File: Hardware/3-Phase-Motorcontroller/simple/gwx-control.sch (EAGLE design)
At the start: 25 parts, among them IC1 74LS02D, IC2 74LS123D

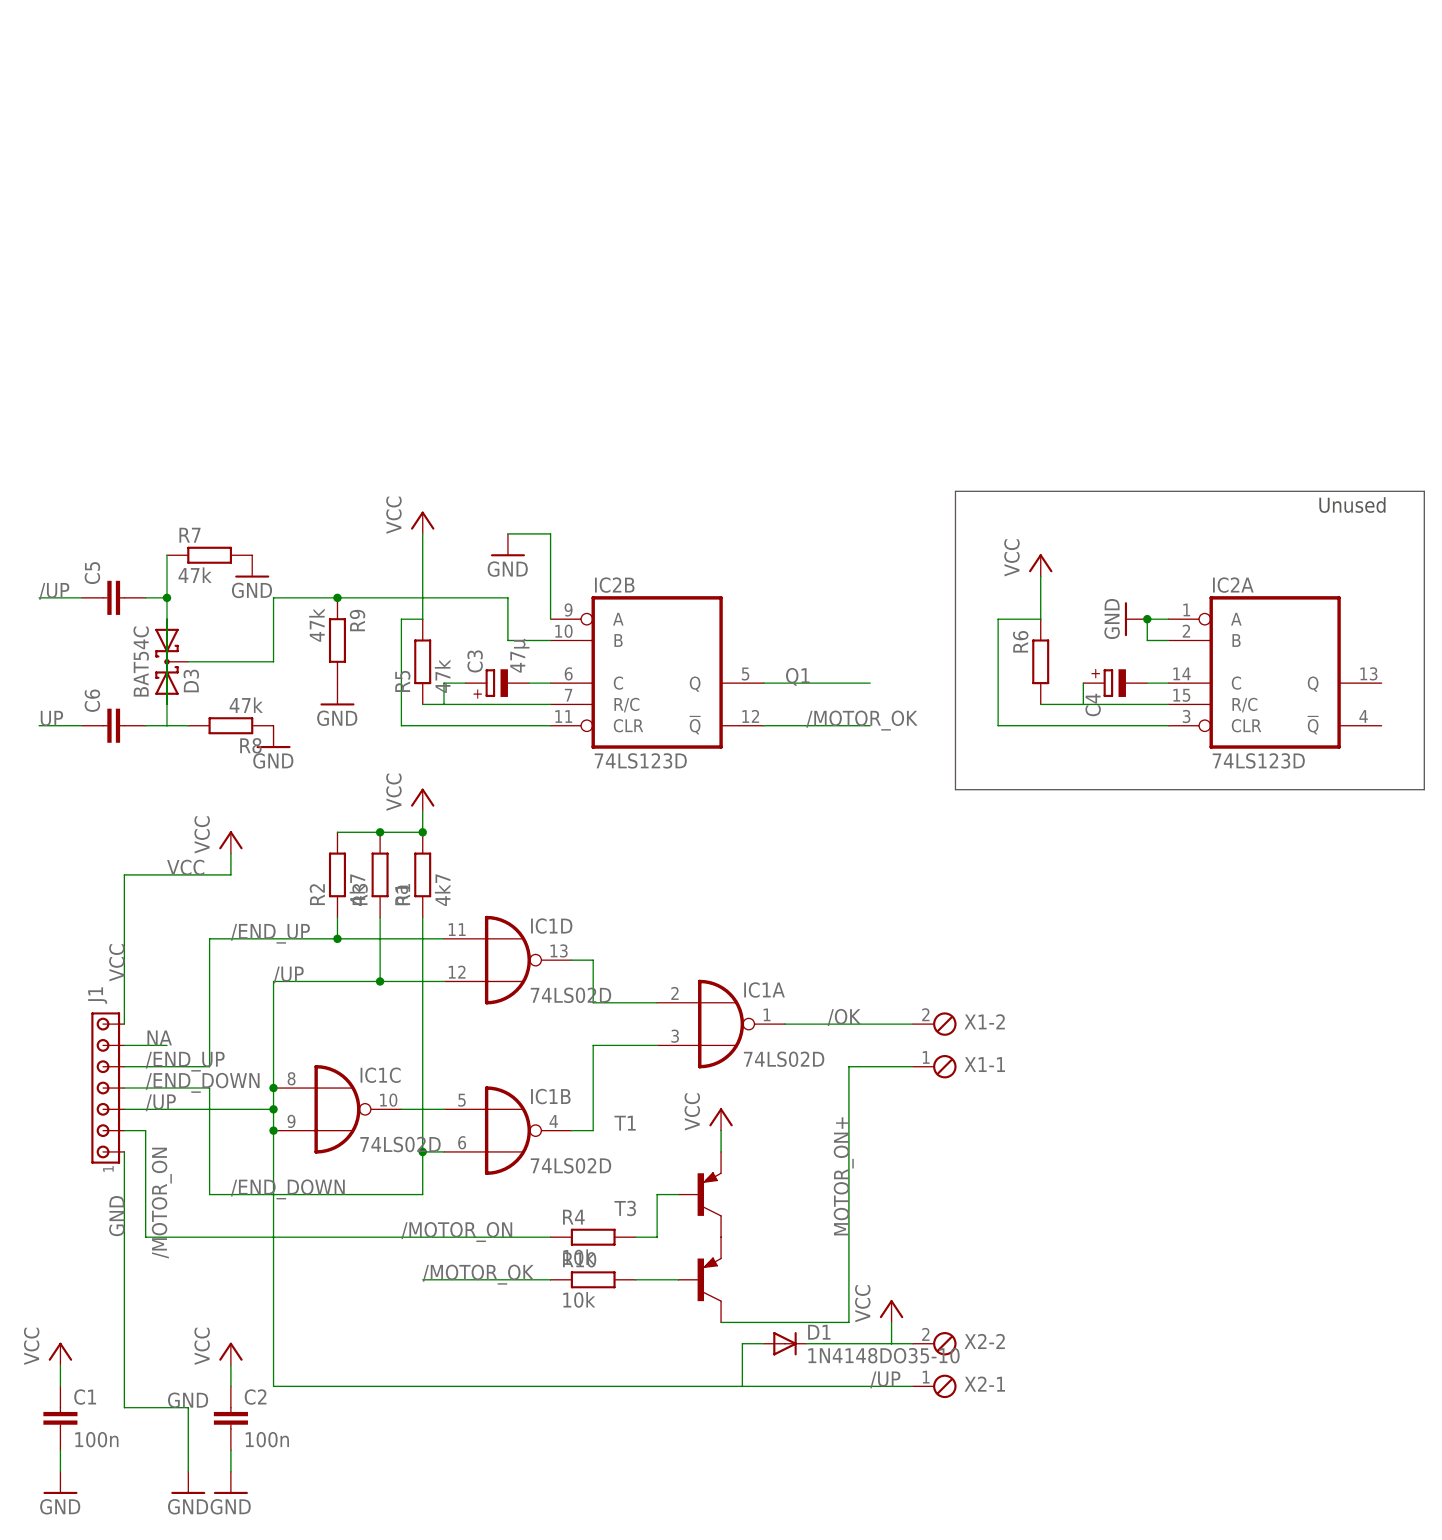
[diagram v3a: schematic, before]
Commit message: Changed Motor force off to non inverted mono flop output
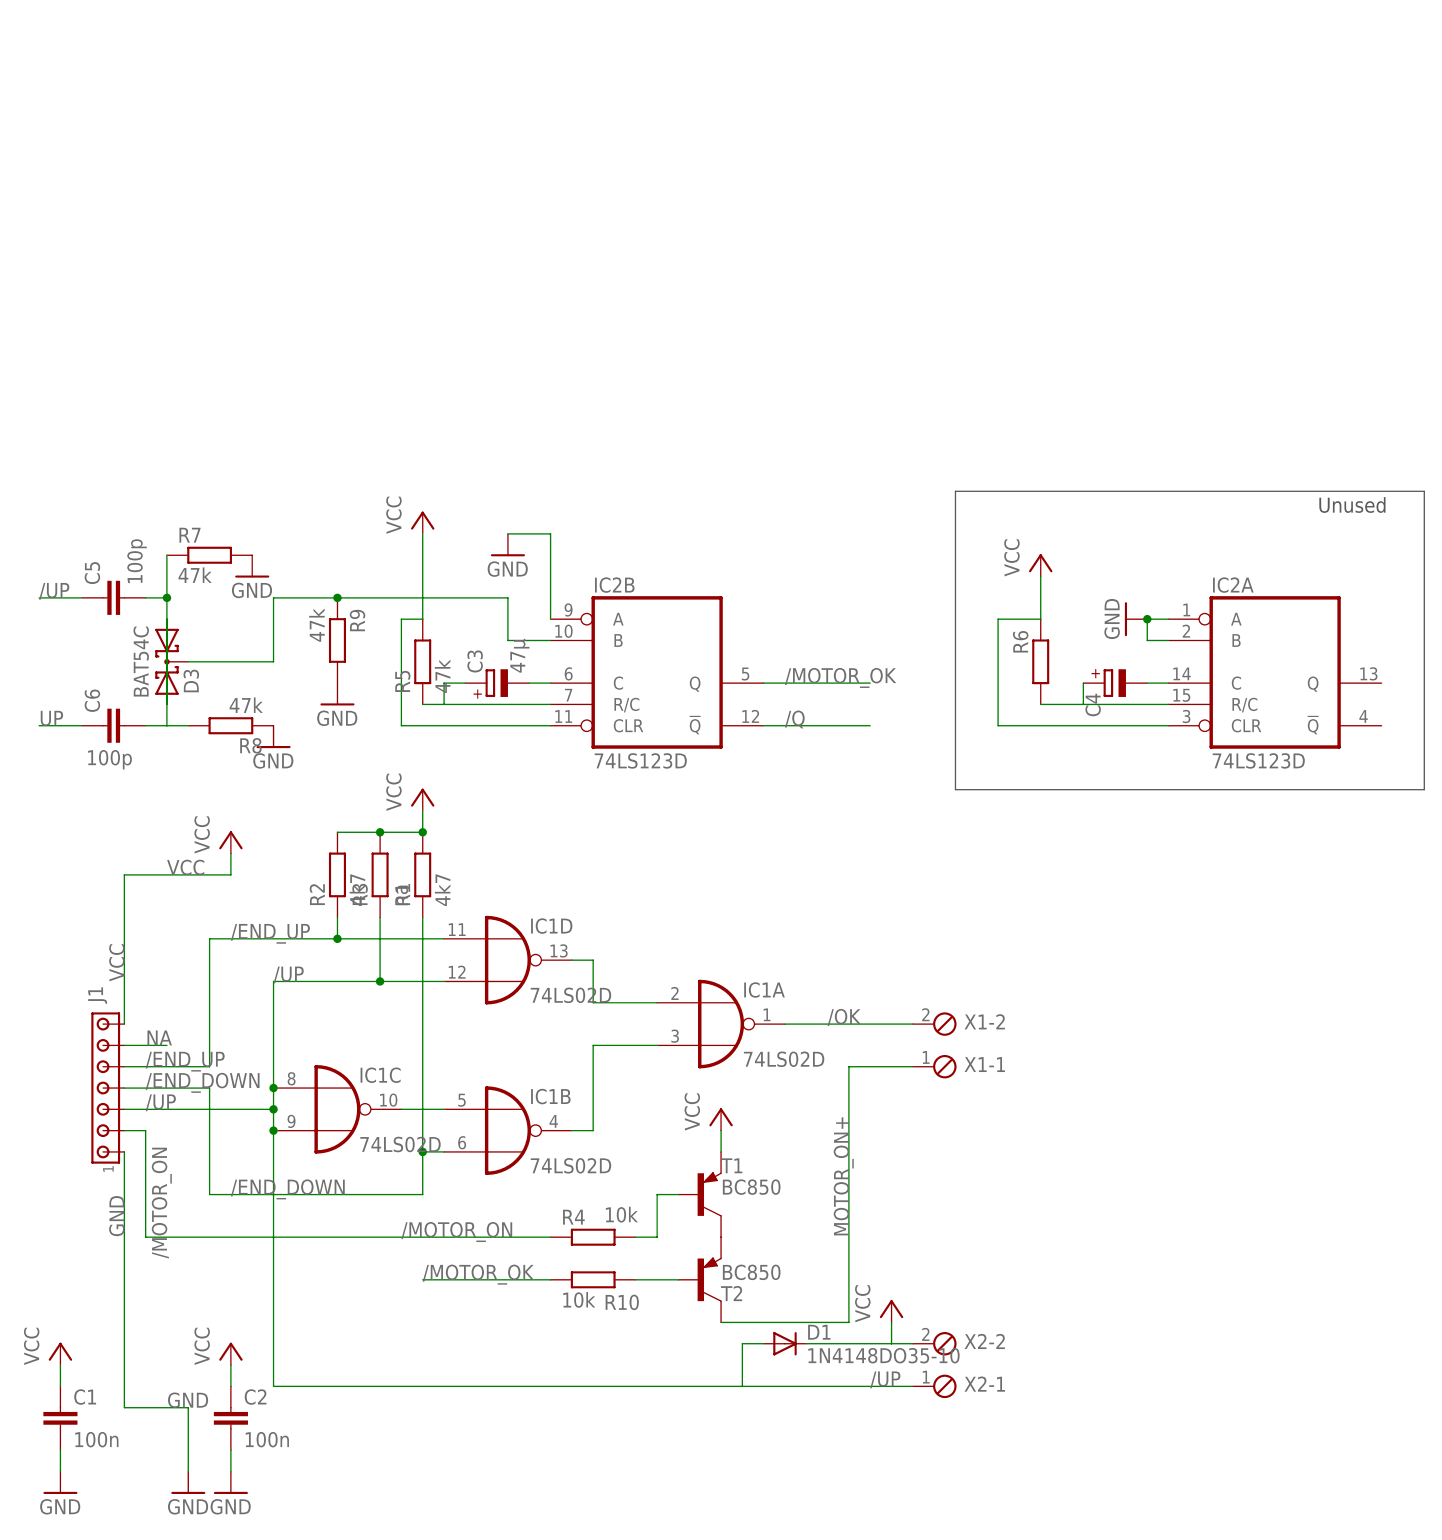
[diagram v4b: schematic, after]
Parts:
- C5, C6: value (none) -> 100p
- T1, T2: value (none) -> BC850
- renumbered T3 to T2
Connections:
- removed net Q1: IC2B.Q
- new net /Q: IC2B.!Q
- net /MOTOR_OK: now also IC2B.Q; no longer IC2B.!Q
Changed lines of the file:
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@@
 <part name="P+4" library="supply1" deviceset="VCC" device=""/>
 <part name="R4" library="resistor" deviceset="R-EU_" device="R0603" value="10k"/>
-<part name="T1" library="transistor" deviceset="*-PNP-" device="SOT23-BEC" technology="BC856B"/>
+<part name="T1" library="transistor" deviceset="*-PNP-" device="SOT23-BEC" technology="BC856B" value="BC850"/>
 <part name="P+5" library="supply1" deviceset="VCC" device=""/>
 <part name="C2" library="rcl" deviceset="C-EU" device="C0603K" value="100n"/>
@@
 <part name="R5" library="rcl" deviceset="R-EU_" device="R0603" value="47k"/>
 <part name="R6" library="rcl" deviceset="R-EU_" device="R0603"/>
-<part name="C5" library="rcl" deviceset="C-EU" device="C0603K"/>
-<part name="C6" library="rcl" deviceset="C-EU" device="C0603K"/>
+<part name="C5" library="rcl" deviceset="C-EU" device="C0603K" value="100p"/>
+<part name="C6" library="rcl" deviceset="C-EU" device="C0603K" value="100p"/>
 <part name="P+7" library="supply1" deviceset="VCC" device=""/>
 <part name="R8" library="rcl" deviceset="R-EU_" device="R0603" value="47k"/>
@@
 <part name="R9" library="rcl" deviceset="R-EU_" device="R0603" value="47k"/>
 <part name="GND8" library="supply1" deviceset="GND" device=""/>
-<part name="T3" library="transistor" deviceset="*-PNP-" device="SOT23-BEC" technology="BC856B"/>
+<part name="T2" library="transistor" deviceset="*-PNP-" device="SOT23-BEC" technology="BC856B" value="BC850"/>
 <part name="R10" library="resistor" deviceset="R-EU_" device="R0603" value="10k"/>
 </parts>
@@
 <instance part="R3" gate="G$1" x="20.32" y="83.82" rot="R90"/>
 <instance part="P+4" gate="VCC" x="25.4" y="93.98"/>
-<instance part="R4" gate="G$1" x="45.72" y="40.64"/>
-<instance part="T1" gate="G$1" x="58.42" y="45.72"/>
+<instance part="R4" gate="G$1" x="45.72" y="40.64" smashed="yes">
+<attribute name="NAME" x="41.91" y="42.1386" size="1.778" layer="95"/>
+<attribute name="VALUE" x="46.99" y="42.418" size="1.778" layer="96"/>
+</instance>
+<instance part="T1" gate="G$1" x="58.42" y="45.72" smashed="yes">
+<attribute name="NAME" x="60.96" y="48.26" size="1.778" layer="95"/>
+<attribute name="VALUE" x="60.96" y="45.72" size="1.778" layer="96"/>
+</instance>
 <instance part="P+5" gate="VCC" x="60.96" y="55.88"/>
 <instance part="C2" gate="G$1" x="2.54" y="20.32"/>
@@
 <instance part="R6" gate="G$1" x="99.06" y="109.22" rot="MR270"/>
 <instance part="C5" gate="G$1" x="-12.7" y="116.84" rot="R90"/>
-<instance part="C6" gate="G$1" x="-12.7" y="101.6" rot="R90"/>
+<instance part="C6" gate="G$1" x="-12.7" y="101.6" smashed="yes" rot="R90">
+<attribute name="NAME" x="-13.081" y="103.124" size="1.778" layer="95" rot="R90"/>
+<attribute name="VALUE" x="-9.144" y="98.679" size="1.778" layer="96" rot="R180"/>
+</instance>
 <instance part="P+7" gate="VCC" x="25.4" y="127"/>
 <instance part="R8" gate="G$1" x="2.54" y="101.6" rot="R180"/>
@@
 <instance part="R9" gate="G$1" x="15.24" y="111.76" rot="R270"/>
 <instance part="GND8" gate="1" x="15.24" y="104.14"/>
-<instance part="T3" gate="G$1" x="58.42" y="35.56"/>
-<instance part="R10" gate="G$1" x="45.72" y="35.56"/>
+<instance part="T2" gate="G$1" x="58.42" y="35.56" smashed="yes">
+<attribute name="NAME" x="60.96" y="33.02" size="1.778" layer="95"/>
+<attribute name="VALUE" x="60.96" y="35.56" size="1.778" layer="96"/>
+</instance>
+<instance part="R10" gate="G$1" x="45.72" y="35.56" smashed="yes">
+<attribute name="NAME" x="46.99" y="31.9786" size="1.778" layer="95"/>
+<attribute name="VALUE" x="41.91" y="32.258" size="1.778" layer="96"/>
+</instance>
 </instances>
 <busses>
@@
 <wire x1="76.2" y1="60.96" x2="76.2" y2="30.48" width="0.1524" layer="91"/>
 <label x="76.2" y="40.64" size="1.778" layer="95" rot="R90"/>
-<pinref part="T3" gate="G$1" pin="C"/>
+<pinref part="T2" gate="G$1" pin="C"/>
 <wire x1="60.96" y1="30.48" x2="76.2" y2="30.48" width="0.1524" layer="91"/>
 </segment>
@@
 <segment>
 <pinref part="T1" gate="G$1" pin="C"/>
-<pinref part="T3" gate="G$1" pin="E"/>
+<pinref part="T2" gate="G$1" pin="E"/>
 </segment>
 </net>
@@
 <segment>
 <pinref part="R10" gate="G$1" pin="2"/>
-<pinref part="T3" gate="G$1" pin="B"/>
+<pinref part="T2" gate="G$1" pin="B"/>
 <wire x1="50.8" y1="35.56" x2="55.88" y2="35.56" width="0.1524" layer="91"/>
 </segment>
@@
 </segment>
 <segment>
-<pinref part="IC2" gate="B" pin="!Q"/>
-<wire x1="66.04" y1="101.6" x2="78.74" y2="101.6" width="0.1524" layer="91"/>
-<label x="71.12" y="101.6" size="1.778" layer="95"/>
-</segment>
-</net>
-<net name="Q1" class="0">
-<segment>
 <pinref part="IC2" gate="B" pin="Q"/>
 <wire x1="66.04" y1="106.68" x2="78.74" y2="106.68" width="0.1524" layer="91"/>
@@
 </segment>
 </net>
+<net name="/Q" class="0">
+<segment>
+<pinref part="IC2" gate="B" pin="!Q"/>
+<wire x1="66.04" y1="101.6" x2="78.74" y2="101.6" width="0.1524" layer="91"/>
+<label x="68.58" y="101.6" size="1.778" layer="95"/>
+</segment>
+</net>

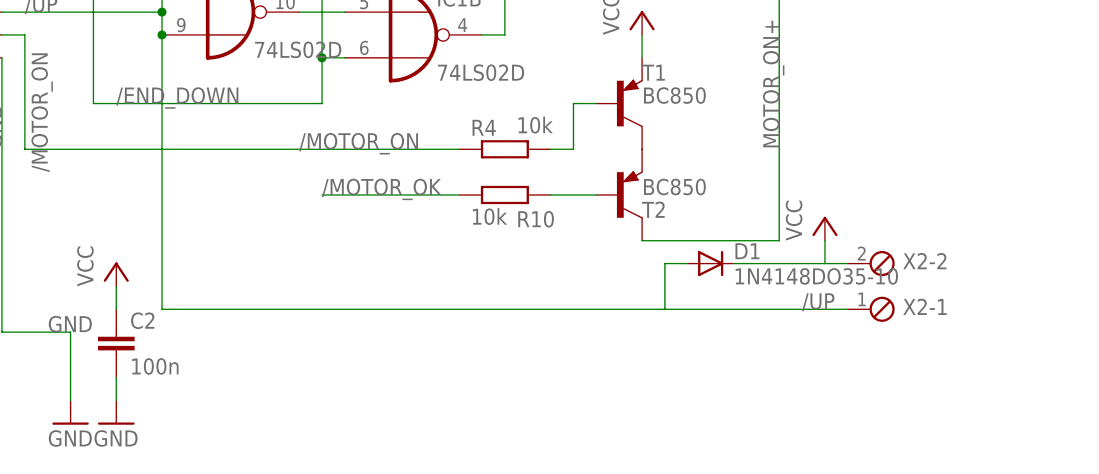
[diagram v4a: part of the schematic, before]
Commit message: added alternative SMD diode
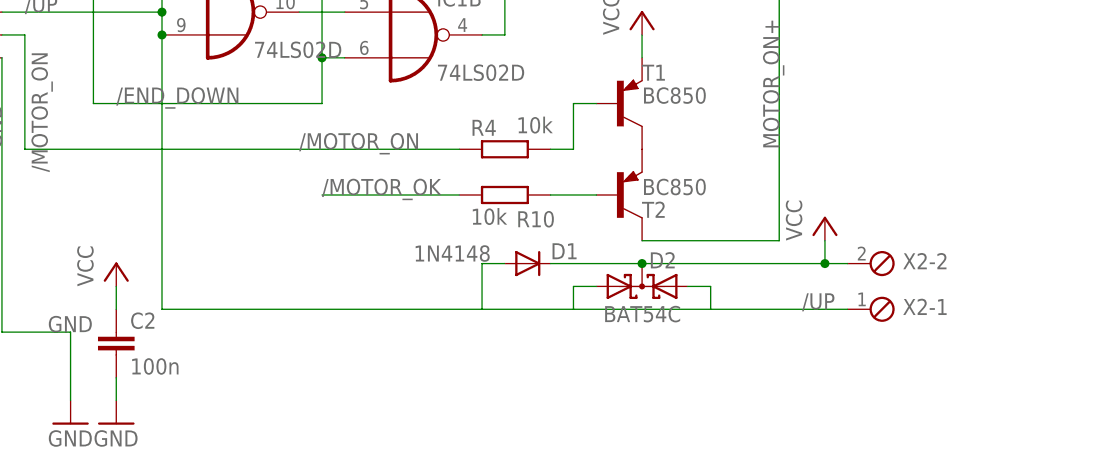
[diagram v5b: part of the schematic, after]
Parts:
- added D2: BAT54C, diode:BAT54C
- D1: value 1N4148DO35-10 -> 1N4148
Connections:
- net /UP: now also D2.A1, D2.A2
- net VCC: now also D2.CC
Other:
- moved on the sheet: D1
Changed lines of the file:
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@@
 <part name="J1" library="con-amp" deviceset="MTA07-100" device=""/>
 <part name="X2" library="con-phoenix-254" deviceset="MPT2" device=""/>
-<part name="D1" library="diode" deviceset="1N4148" device="DO35-10"/>
+<part name="D1" library="diode" deviceset="1N4148" device="DO35-10" value="1N4148"/>
 <part name="R1" library="resistor" deviceset="R-EU_" device="R0603" value="4k7"/>
 <part name="R2" library="resistor" deviceset="R-EU_" device="R0603" value="4k7"/>
@@
 <part name="T2" library="transistor" deviceset="*-PNP-" device="SOT23-BEC" technology="BC856B" value="BC850"/>
 <part name="R10" library="resistor" deviceset="R-EU_" device="R0603" value="10k"/>
+<part name="D2" library="diode" deviceset="BAT54C" device=""/>
 </parts>
 <sheets>
@@
 <instance part="X2" gate="-1" x="86.36" y="22.86"/>
 <instance part="X2" gate="-2" x="86.36" y="27.94"/>
-<instance part="D1" gate="G$1" x="68.58" y="27.94"/>
+<instance part="D1" gate="G$1" x="48.26" y="27.94" smashed="yes">
+<attribute name="NAME" x="50.8" y="28.4226" size="1.778" layer="95"/>
+<attribute name="VALUE" x="35.56" y="28.1686" size="1.778" layer="96"/>
+</instance>
 <instance part="R1" gate="G$1" x="25.4" y="83.82" rot="R90"/>
 <instance part="R2" gate="G$1" x="15.24" y="83.82" rot="R90"/>
@@
 <attribute name="VALUE" x="41.91" y="32.258" size="1.778" layer="96"/>
 </instance>
+<instance part="D2" gate="G$1" x="60.96" y="25.4"/>
 </instances>
 <busses>
@@
 <wire x1="7.62" y1="53.34" x2="7.62" y2="22.86" width="0.1524" layer="91"/>
 <junction x="7.62" y="53.34"/>
-<pinref part="D1" gate="G$1" pin="A"/>
-<wire x1="63.5" y1="22.86" x2="7.62" y2="22.86" width="0.1524" layer="91"/>
-<wire x1="66.04" y1="27.94" x2="63.5" y2="27.94" width="0.1524" layer="91"/>
-<wire x1="63.5" y1="27.94" x2="63.5" y2="22.86" width="0.1524" layer="91"/>
+<wire x1="83.82" y1="22.86" x2="68.58" y2="22.86" width="0.1524" layer="91"/>
 <pinref part="R3" gate="G$1" pin="1"/>
+<wire x1="68.58" y1="22.86" x2="53.34" y2="22.86" width="0.1524" layer="91"/>
+<wire x1="53.34" y1="22.86" x2="43.18" y2="22.86" width="0.1524" layer="91"/>
+<wire x1="43.18" y1="22.86" x2="7.62" y2="22.86" width="0.1524" layer="91"/>
 <wire x1="20.32" y1="78.74" x2="20.32" y2="71.12" width="0.1524" layer="91"/>
 <junction x="20.32" y="71.12"/>
@@
 <label x="78.74" y="22.86" size="1.778" layer="95"/>
 <pinref part="X2" gate="-1" pin="1"/>
-<wire x1="63.5" y1="22.86" x2="83.82" y2="22.86" width="0.1524" layer="91"/>
+<pinref part="D1" gate="G$1" pin="A"/>
+<wire x1="45.72" y1="27.94" x2="43.18" y2="27.94" width="0.1524" layer="91"/>
+<wire x1="43.18" y1="27.94" x2="43.18" y2="22.86" width="0.1524" layer="91"/>
+<pinref part="D2" gate="G$1" pin="A1"/>
+<wire x1="55.88" y1="25.4" x2="53.34" y2="25.4" width="0.1524" layer="91"/>
+<wire x1="53.34" y1="25.4" x2="53.34" y2="22.86" width="0.1524" layer="91"/>
+<pinref part="D2" gate="G$1" pin="A2"/>
+<wire x1="66.04" y1="25.4" x2="68.58" y2="25.4" width="0.1524" layer="91"/>
+<wire x1="68.58" y1="25.4" x2="68.58" y2="22.86" width="0.1524" layer="91"/>
 </segment>
 <segment>
@@
 <wire x1="81.28" y1="27.94" x2="81.28" y2="30.48" width="0.1524" layer="91"/>
 <pinref part="D1" gate="G$1" pin="C"/>
-<wire x1="71.12" y1="27.94" x2="81.28" y2="27.94" width="0.1524" layer="91"/>
+<wire x1="50.8" y1="27.94" x2="60.96" y2="27.94" width="0.1524" layer="91"/>
 <pinref part="X2" gate="-2" pin="1"/>
+<wire x1="60.96" y1="27.94" x2="81.28" y2="27.94" width="0.1524" layer="91"/>
 <wire x1="81.28" y1="27.94" x2="83.82" y2="27.94" width="0.1524" layer="91"/>
-</segment>
-<segment>
+<pinref part="D2" gate="G$1" pin="CC"/>
+<junction x="60.96" y="27.94"/>
+<junction x="81.28" y="27.94"/>
+</segment>
+<segment>
